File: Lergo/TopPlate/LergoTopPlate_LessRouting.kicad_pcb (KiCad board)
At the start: 2 copper layers, 164 x 146.3 mm, 45 parts, among them SW2 KEY_SWITCH, SW2 PRO MICRO

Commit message: Pimoroni spelling is hard :D
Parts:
- REF**: value Pimonori_Trackball -> Pimoroni_Trackball; footprint Lergo Footprints:Pimonori_Trackball -> Lergo Footprints:Pimoroni_Trackball

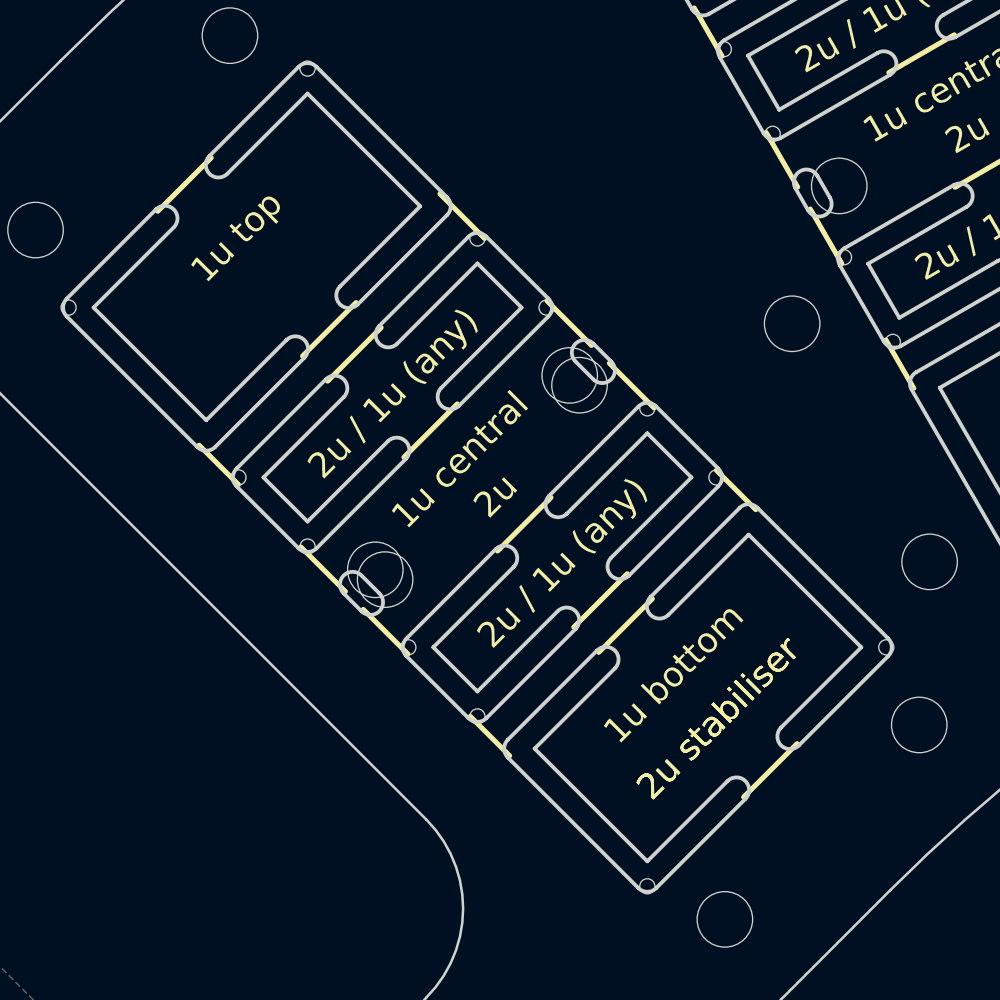
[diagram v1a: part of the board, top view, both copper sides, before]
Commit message: Integrating Pimoroni trackball in all top plates.
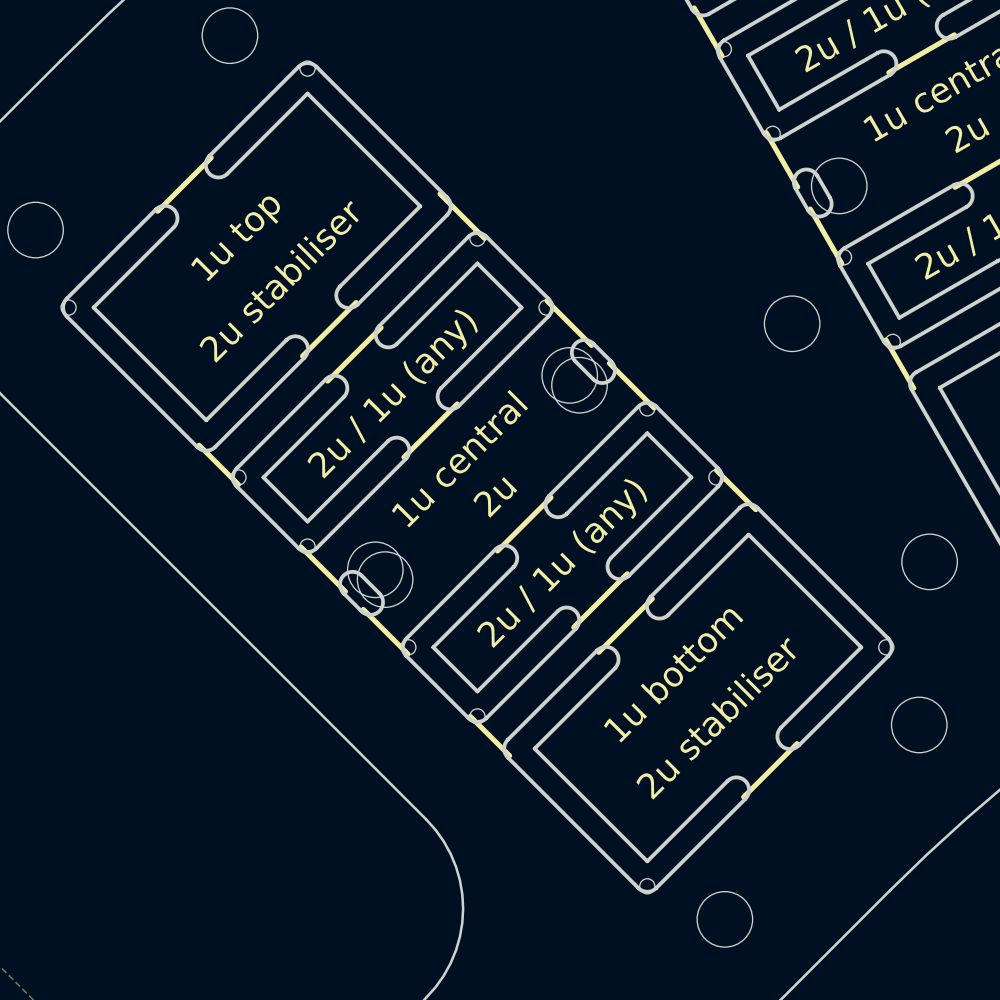
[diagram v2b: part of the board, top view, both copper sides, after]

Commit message: Extended silkscreen for roller encoder on all pre-drilled encoder positions.
Also, doubled the pre-drills rotated 90 degrees for easier mounting of roller encoder in alternate direction.
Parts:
- added REF**: RollerEncoder_Panasonic_EVQWGD001, Lergo Footprints:RollerEncoder_TopPlate, F.Cu at (226.2, 53.4)
- added REF**: RollerEncoder_Panasonic_EVQWGD001, Lergo Footprints:RollerEncoder_TopPlate, F.Cu at (226.2, 72.5)
- added REF**: RollerEncoder_Panasonic_EVQWGD001, Lergo Footprints:RollerEncoder_TopPlate, F.Cu at (226.2, 91.5)
- added REF**: RollerEncoder_Panasonic_EVQWGD001, Lergo Footprints:RollerEncoder_TopPlate, F.Cu at (226.2, 110.5)
- added REF**: RollerEncoder_Panasonic_EVQWGD001, Lergo Footprints:RollerEncoder_TopPlate, F.Cu at (180.8, 118.1)
- added REF**: RollerEncoder_Panasonic_EVQWGD001, Lergo Footprints:RollerEncoder_TopPlate, F.Cu at (161.8, 118.1)
- REF**: moved to B.Cu
- turned REF** to 15 degrees
- turned REF** to 195 degrees
